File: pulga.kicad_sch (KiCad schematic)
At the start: 28 parts, among them J1 Conn_01x04_Pin, SW1 SW_Push, SW2 SW_Push, U2 ESP32-C3-WROOM-02, U3 TCAN332G

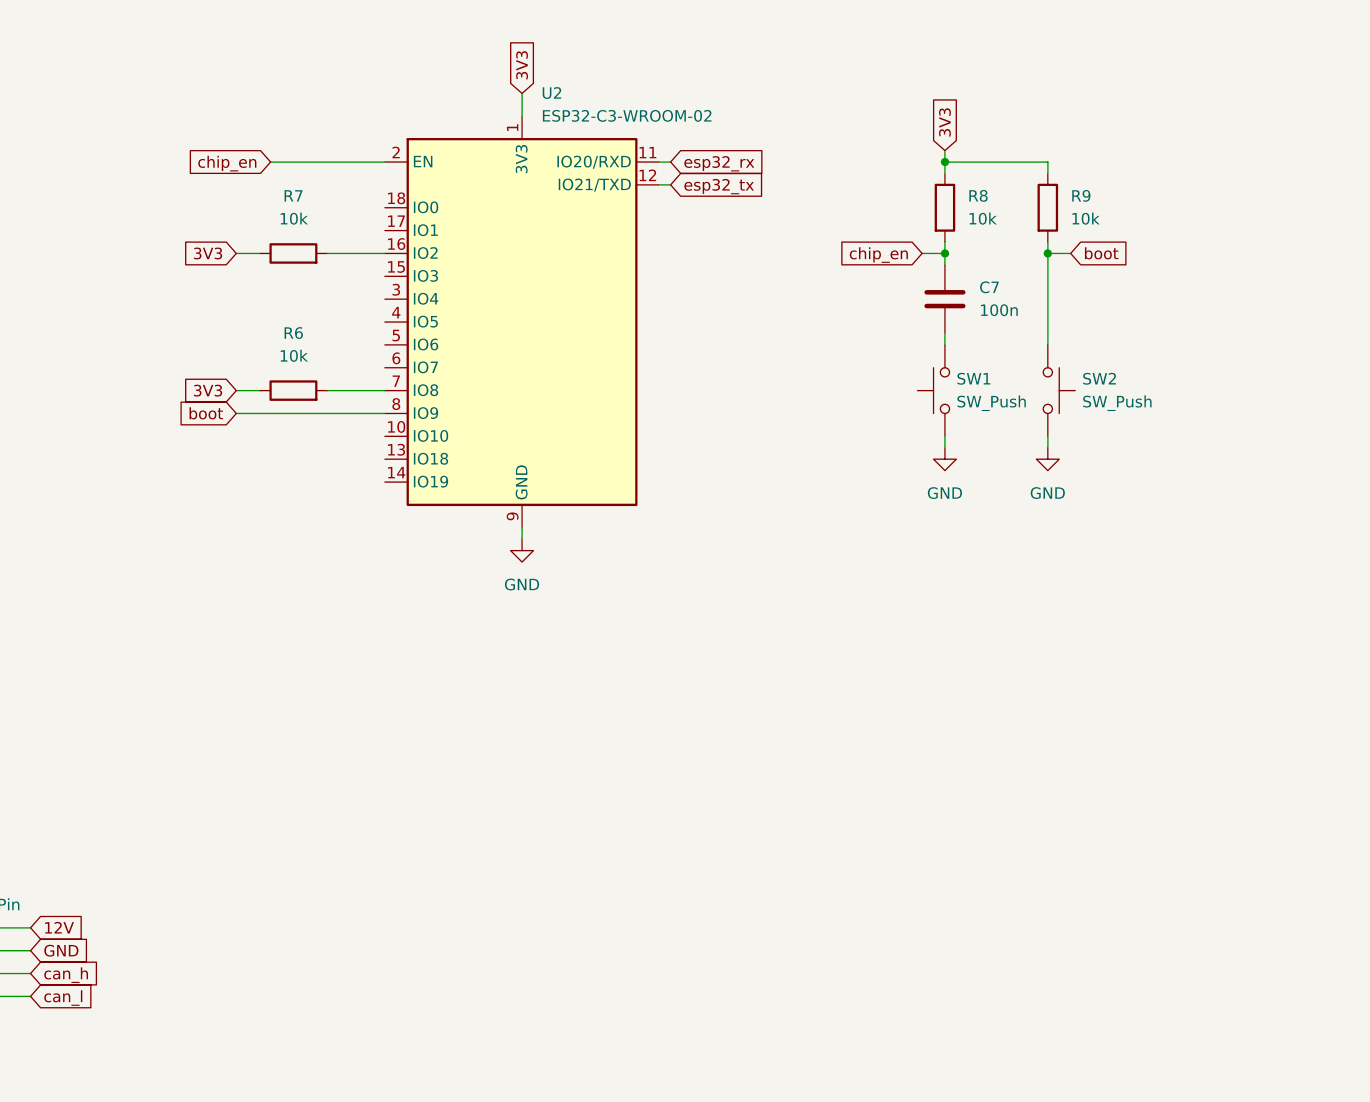
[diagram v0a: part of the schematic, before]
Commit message: ajeitando os pinos de conexão do OBD
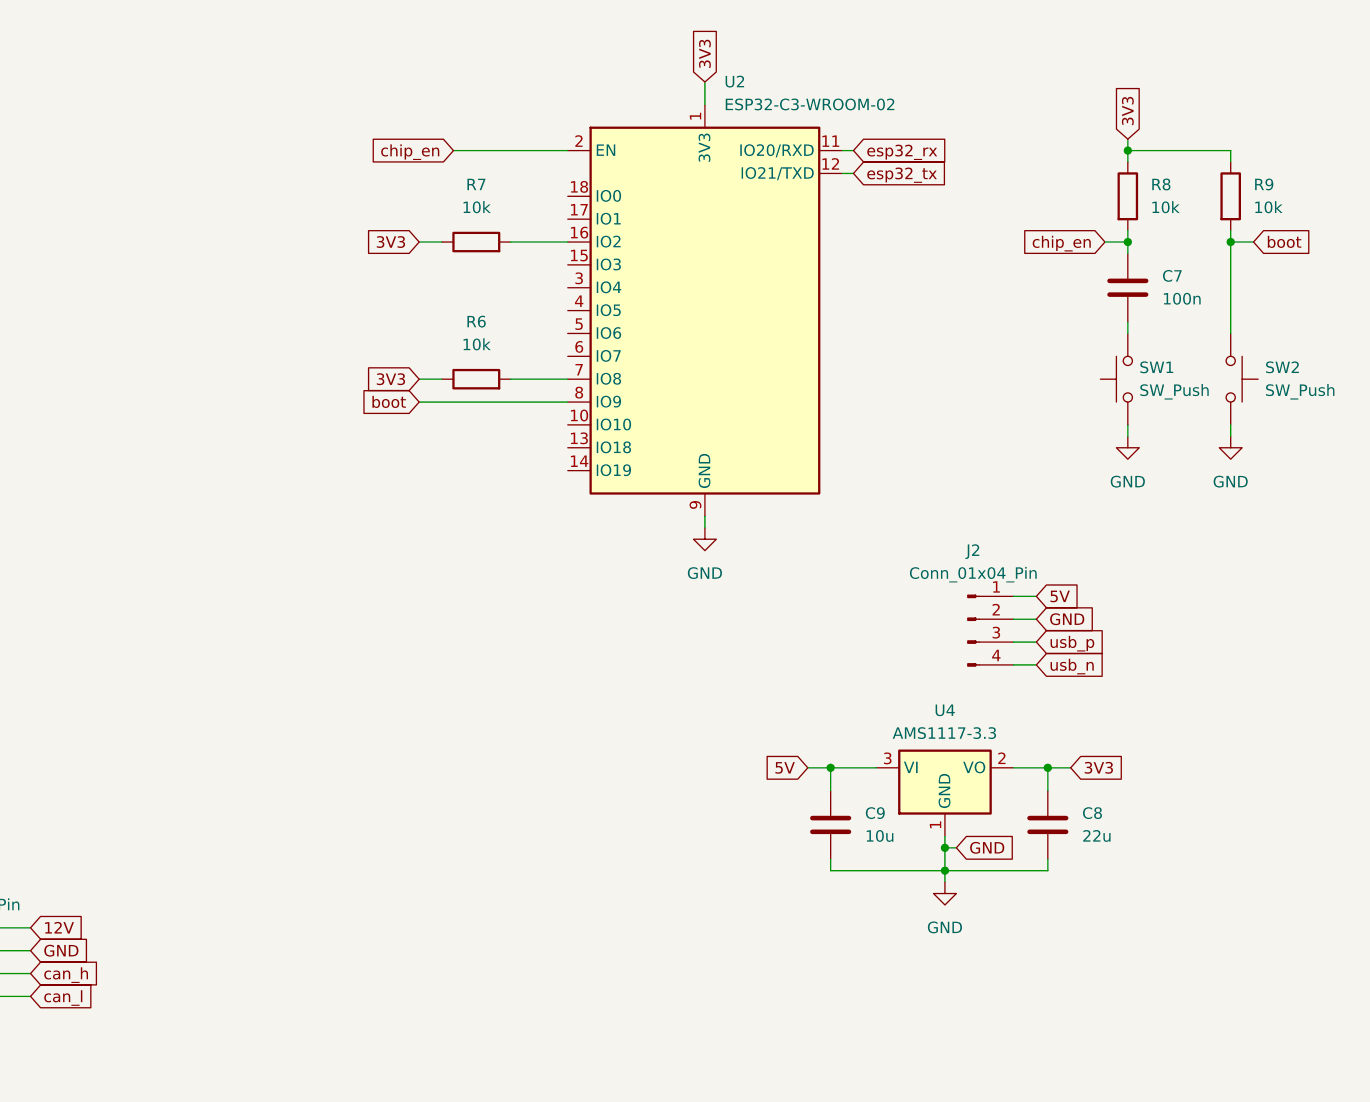
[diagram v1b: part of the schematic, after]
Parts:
- added C8: 22u, Capacitor_SMD:C_1206_3216Metric, symbol Device:C
- added C9: 10u, Capacitor_SMD:C_1206_3216Metric, symbol Device:C
- added J2: Conn_01x04_Pin, symbol Connector:Conn_01x04_Pin
- added U4: AMS1117-3.3, Package_TO_SOT_SMD:SOT-223-3_TabPin2, symbol Regulator_Linear:AMS1117-3.3
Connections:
- net 3V3: now also C8.1, U4.2 (VO)
- net GND: now also C8.2, C9.2, J2.2 (Pin_2), U4.1 (GND)
- new net 5V: C9.1, J2.1 (Pin_1), U4.3 (VI)
- new net usb_n: J2.4 (Pin_4)
- new net usb_p: J2.3 (Pin_3)
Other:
- moved on the sheet: C7, R6, R7, R8, R9, SW1, SW2, U2

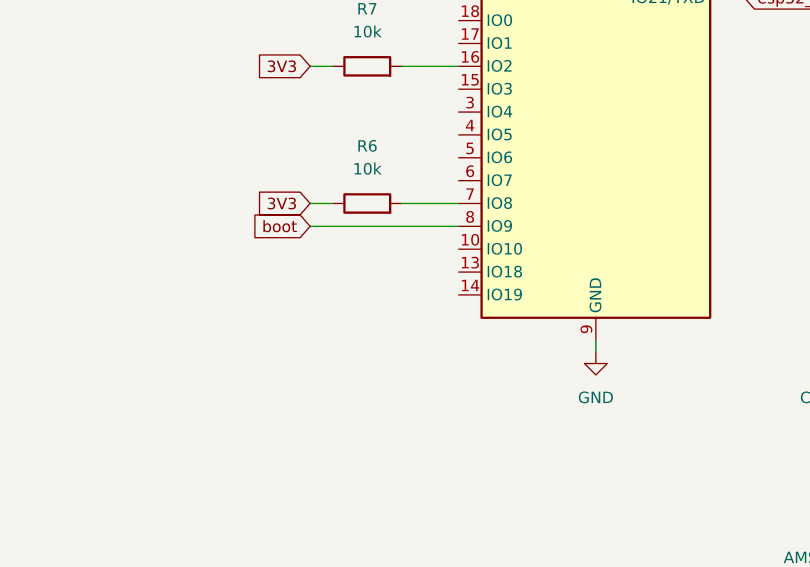
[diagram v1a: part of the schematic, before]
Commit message: adicionando as conexões 5v, GND, USB_(P|N) e o LDO
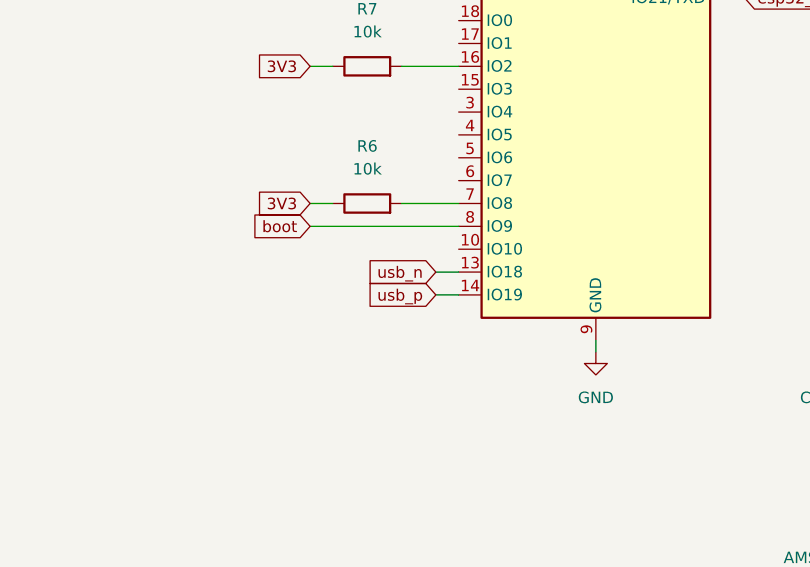
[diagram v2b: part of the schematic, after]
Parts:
- J2: footprint (none) -> through_hole:obd_main_pins
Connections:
- net usb_n: now also U2.13 (IO18)
- net usb_p: now also U2.14 (IO19)
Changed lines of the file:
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@@
+	(wire
+		(pts
+			(xy 191.77 60.96) (xy 194.31 60.96)
+		)
+		(stroke
+			(width 0)
+			(type default)
+		)
+	)
 	(wire
 		(pts
@@
 	(wire
 		(pts
+			(xy 191.77 63.5) (xy 194.31 63.5)
+		)
+		(stroke
+			(width 0)
+			(type default)
+		)
+	)
+	(wire
+		(pts
 			(xy 114.3 26.67) (xy 113.03 26.67)
 		)
@@
 				)
 				(justify left)
+				(hide yes)
+			)
+		)
+	)
+	(global_label "usb_p"
+		(shape input)
+		(at 191.77 63.5 180)
+		(fields_autoplaced yes)
+		(effects
+			(font
+				(size 1.27 1.27)
+			)
+			(justify right)
+		)
+		(property "Intersheetrefs" "${INTERSHEET_REFS}"
+			(at 183.3421 63.5 0)
+			(effects
+				(font
+					(size 1.27 1.27)
+				)
+				(justify right)
+				(hide yes)
+			)
+		)
+	)
+	(global_label "usb_n"
+		(shape input)
+		(at 191.77 60.96 180)
+		(fields_autoplaced yes)
+		(effects
+			(font
+				(size 1.27 1.27)
+			)
+			(justify right)
+		)
+		(property "Intersheetrefs" "${INTERSHEET_REFS}"
+			(at 183.3421 60.96 0)
+			(effects
+				(font
+					(size 1.27 1.27)
+				)
+				(justify right)
 				(hide yes)
 			)
@@
 			)
 		)
-		(property "Footprint" ""
+		(property "Footprint" "through_hole:obd_main_pins"
 			(at 238.76 80.01 0)
 			(effects

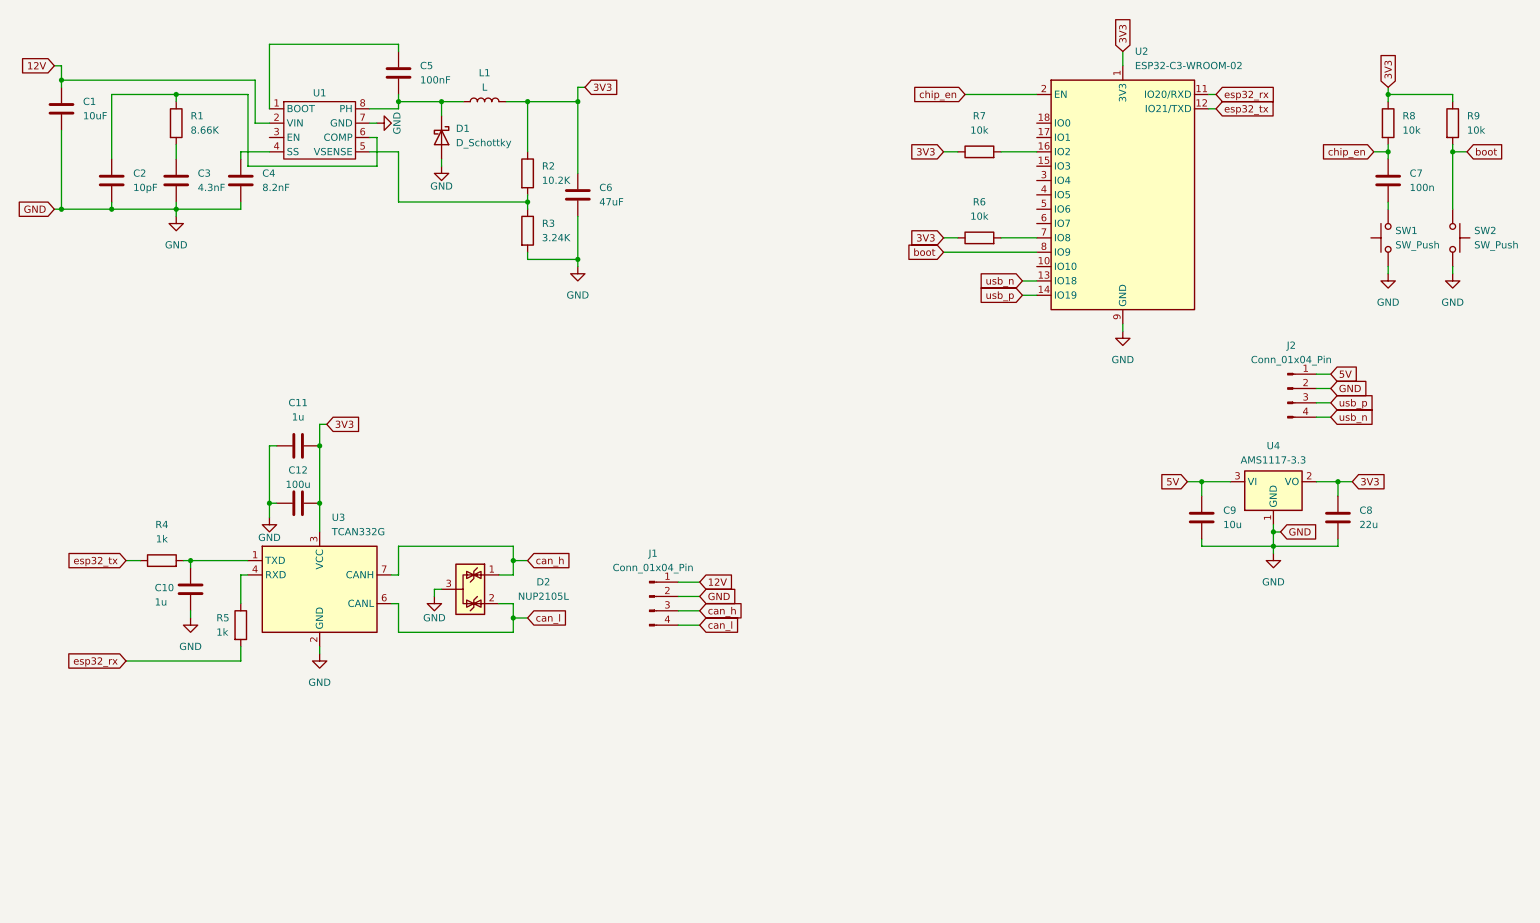
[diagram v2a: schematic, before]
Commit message: centralizando o módulo na folha de PCB e dando nomes as partes no SCH
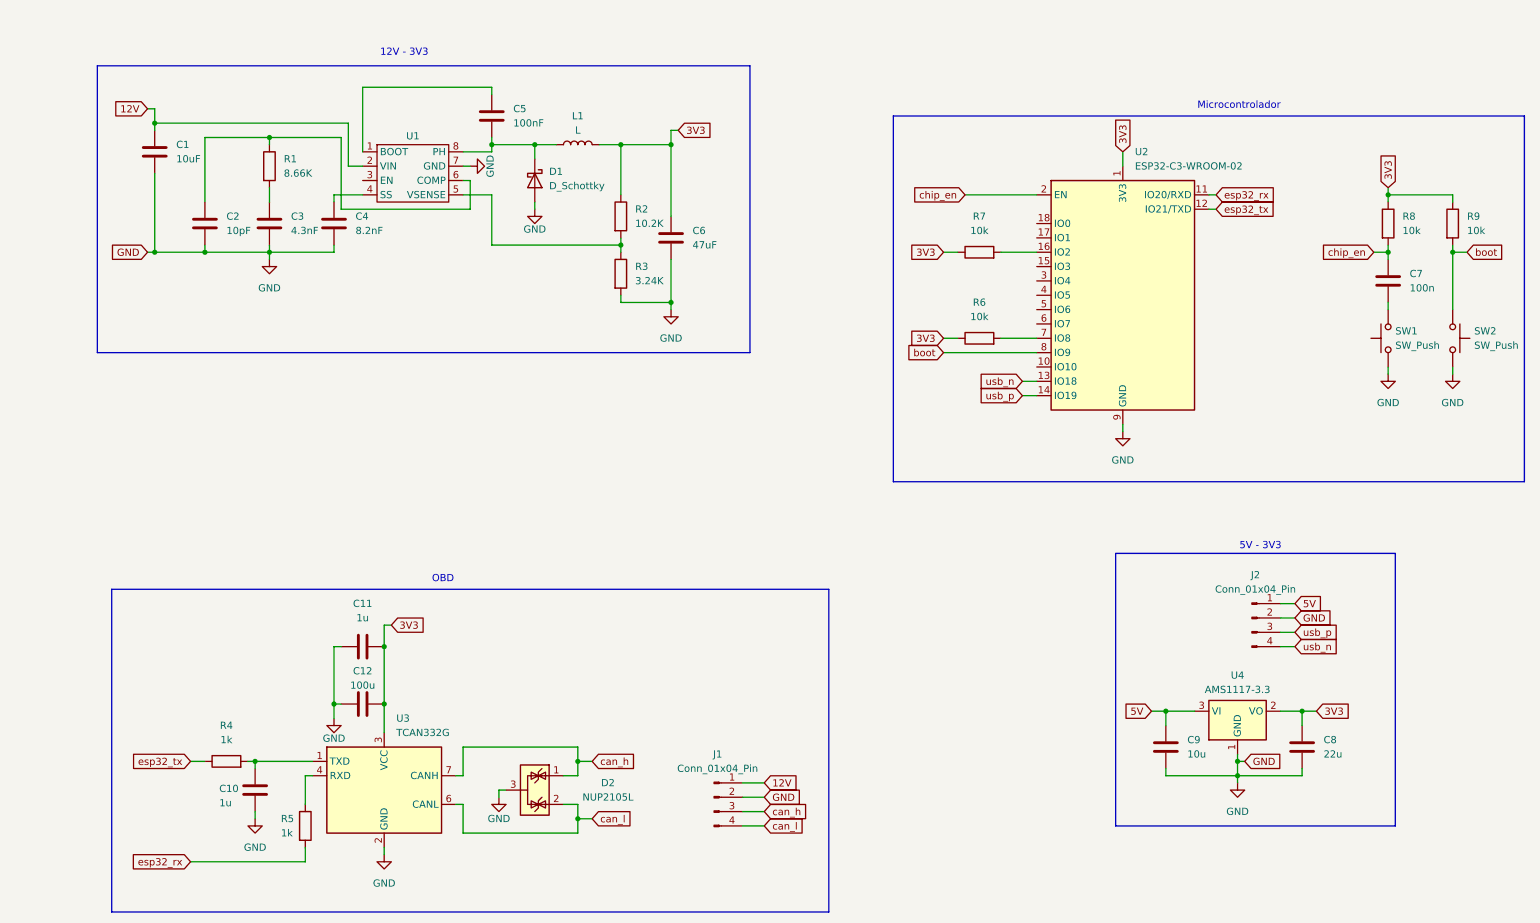
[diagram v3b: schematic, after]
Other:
- note added: "12V - 3V3"
- note added: "5V - 3V3"
- note added: "Microcontrolador"
- note added: "OBD"
- moved on the sheet: C1, C10, C11, C12, C2, C3, C4, C5, C6, C7, C8, C9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

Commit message: adicionando o LCSC aos resistores
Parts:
- R1: LCSC (none) -> C185387
- R2: LCSC (none) -> C11660
- R3: LCSC (none) -> C22369275
- R4, R5: LCSC (none) -> C22369184
- R6, R7, R8, R9: LCSC (none) -> C102690
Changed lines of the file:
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@@
+			)
+		)
+		(property "LCSC" "C22369275"
+			(at 120.65 59.69 0)
+			(effects
+				(font
+					(size 1.27 1.27)
+				)
+				(hide yes)
 			)
 		)
@@
 			)
 		)
+		(property "LCSC" "C185387"
+			(at 58.42 40.64 0)
+			(effects
+				(font
+					(size 1.27 1.27)
+				)
+				(hide yes)
+			)
+		)
 		(pin "2"
 		)
@@
 			)
 		)
+		(property "LCSC" "C102690"
+			(at 267.97 50.8 0)
+			(effects
+				(font
+					(size 1.27 1.27)
+				)
+				(hide yes)
+			)
+		)
 		(pin "2"
 		)
@@
 			)
 		)
+		(property "LCSC" "C22369184"
+			(at 50.8 146.05 90)
+			(effects
+				(font
+					(size 1.27 1.27)
+				)
+				(hide yes)
+			)
+		)
 		(pin "2"
 		)
@@
 			)
 		)
+		(property "LCSC" "C102690"
+			(at 184.15 71.12 90)
+			(effects
+				(font
+					(size 1.27 1.27)
+				)
+				(hide yes)
+			)
+		)
 		(pin "2"
 		)
@@
 			)
 		)
+		(property "LCSC" "C11660"
+			(at 120.65 49.53 0)
+			(effects
+				(font
+					(size 1.27 1.27)
+				)
+				(hide yes)
+			)
+		)
 		(pin "2"
 		)
@@
 			)
 		)
+		(property "LCSC" "C102690"
+			(at 184.15 55.88 90)
+			(effects
+				(font
+					(size 1.27 1.27)
+				)
+				(hide yes)
+			)
+		)
 		(pin "2"
 		)
@@
 			)
 		)
+		(property "LCSC" "C102690"
+			(at 256.54 50.8 0)
+			(effects
+				(font
+					(size 1.27 1.27)
+				)
+				(hide yes)
+			)
+		)
 		(pin "2"
 		)
@@
 			(at 64.77 157.48 0)
 			(effects
+				(font
+					(size 1.27 1.27)
+				)
+				(hide yes)
+			)
+		)
+		(property "LCSC" "C22369184"
+			(at 64.77 157.48 0)
+			(effects

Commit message: adicionando o LCSC aos componentes do circuito de alimentação 12V-3.3V
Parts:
- C1: LCSC (none) -> C39232
- C2: LCSC (none) -> C107107
- C3: LCSC (none) -> C3885982
- C4: LCSC (none) -> C2168104
- C5: LCSC (none) -> C86041
- C6: LCSC (none) -> C77101
- D1: footprint Diode_SMD:D_SMF -> Diode_SMD:D_SMA; LCSC (none) -> C47460
- L1: LCSC (none) -> C3224592
- U1: LCSC (none) -> C544741
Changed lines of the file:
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@@
 			)
 		)
-		(property "Footprint" "Diode_SMD:D_SMF"
+		(property "Footprint" "Diode_SMD:D_SMA"
 			(at 105.41 43.18 0)
 			(effects
@@
 			)
 		)
-		(property "Datasheet" "https://download.siliconexpert.com/pdfs/2016/6/23/7/52/25/619/vsh_/manual/701582923671303sl02.pdf"
+		(property "Datasheet" "https://jlcpcb.com/api/file/downloadByFileSystemAccessId/8586176510520659968"
 			(at 105.41 43.18 0)
 			(effects
@@
 			)
 		)
+		(property "LCSC" "C47460"
+			(at 105.41 43.18 90)
+			(effects
+				(font
+					(size 1.27 1.27)
+				)
+				(hide yes)
+			)
+		)
 		(pin "2"
 		)
@@
 			)
 		)
+		(property "LCSC" "C3224592"
+			(at 113.03 36.83 90)
+			(effects
+				(font
+					(size 1.27 1.27)
+				)
+				(hide yes)
+			)
+		)
 		(pin "2"
 		)
@@
 			)
 		)
+		(property "LCSC" "C77101"
+			(at 129.54 53.34 0)
+			(effects
+				(font
+					(size 1.27 1.27)
+				)
+				(hide yes)
+			)
+		)
 		(pin "1"
 		)
@@
 			)
 		)
+		(property "LCSC" "C544741"
+			(at 83.82 41.91 0)
+			(effects
+				(font
+					(size 1.27 1.27)
+				)
+				(hide yes)
+			)
+		)
 		(pin "6"
 		)
@@
 			)
 		)
+		(property "LCSC" "C39232"
+			(at 38.1 38.1 0)
+			(effects
+				(font
+					(size 1.27 1.27)
+				)
+				(hide yes)
+			)
+		)
 		(pin "1"
 		)
@@
 			)
 		)
+		(property "LCSC" "C3885982"
+			(at 58.42 50.8 0)
+			(effects
+				(font
+					(size 1.27 1.27)
+				)
+				(hide yes)
+			)
+		)
 		(pin "1"
 		)
@@
 			)
 		)
+		(property "LCSC" "C2168104"
+			(at 69.85 50.8 0)
+			(effects
+				(font
+					(size 1.27 1.27)
+				)
+				(hide yes)
+			)
+		)
 		(pin "1"
 		)
@@
 			)
 		)
+		(property "LCSC" "C107107"
+			(at 46.99 50.8 0)
+			(effects
+				(font
+					(size 1.27 1.27)
+				)
+				(hide yes)
+			)
+		)
 		(pin "1"
 		)
@@
 			(at 97.79 31.75 0)
 			(effects
+				(font
+					(size 1.27 1.27)
+				)
+				(hide yes)
+			)
+		)
+		(property "LCSC" "C86041"
+			(at 97.79 31.75 0)
+			(effects
